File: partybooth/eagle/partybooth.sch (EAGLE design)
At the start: 21 parts, among them IC1 TINY13-20PU, IC2 78L05Z, J1 Lamp, J2 Button, J3 12V, T1 2N3904, T2 2N3904, X1 1501_06

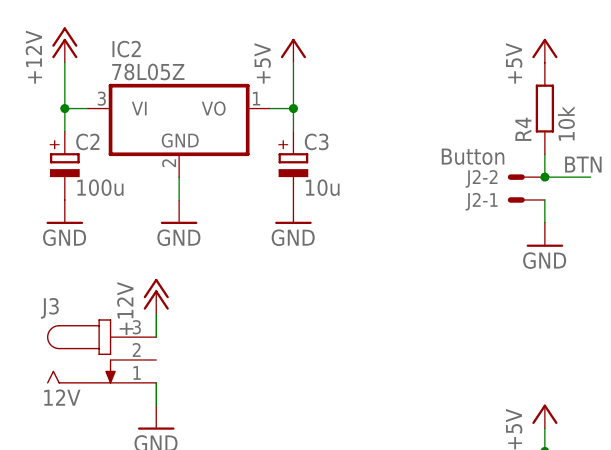
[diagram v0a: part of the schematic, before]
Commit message: 
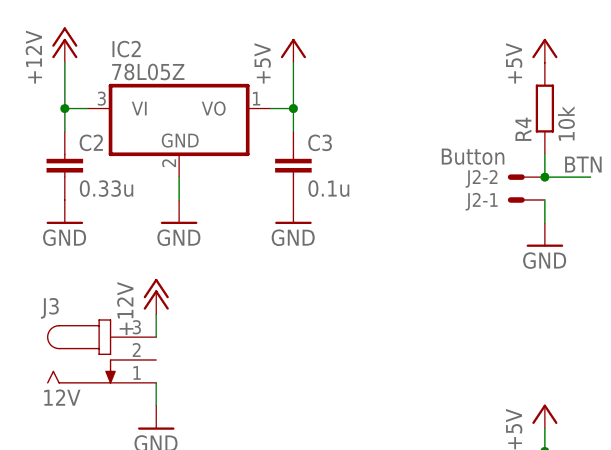
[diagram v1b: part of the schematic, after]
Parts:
- C2: value 100u -> 0.33u; device rcl:CPOL-EUB45181B -> rcl:C-EU050-025X075
- C3: value 10u -> 0.1u; device rcl:CPOL-EUB45181B -> rcl:C-EU050-025X075
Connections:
- net +12V: now also C2.1; no longer C2.+
- net +5V: now also C3.1; no longer C3.+
- net GND: now also C2.2, C3.2; no longer C2.-, C3.-
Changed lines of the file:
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@@
 <grid distance="0.1" unitdist="inch" unit="inch" style="lines" multiple="1" display="no" altdistance="0.01" altunitdist="inch" altunit="inch"/>
 <layers>
-<layer number="1" name="Top" color="4" fill="1" visible="yes" active="no"/>
-<layer number="2" name="Route2" color="1" fill="3" visible="yes" active="no"/>
-<layer number="3" name="Route3" color="4" fill="3" visible="yes" active="no"/>
-<layer number="14" name="Route14" color="1" fill="6" visible="yes" active="no"/>
-<layer number="15" name="Route15" color="4" fill="6" visible="yes" active="no"/>
-<layer number="16" name="Bottom" color="1" fill="1" visible="yes" active="no"/>
-<layer number="17" name="Pads" color="2" fill="1" visible="yes" active="no"/>
-<layer number="18" name="Vias" color="2" fill="1" visible="yes" active="no"/>
-<layer number="19" name="Unrouted" color="6" fill="1" visible="yes" active="no"/>
-<layer number="20" name="Dimension" color="15" fill="1" visible="yes" active="no"/>
-<layer number="21" name="tPlace" color="7" fill="1" visible="yes" active="no"/>
-<layer number="22" name="bPlace" color="7" fill="1" visible="yes" active="no"/>
-<layer number="23" name="tOrigins" color="15" fill="1" visible="yes" active="no"/>
-<layer number="24" name="bOrigins" color="15" fill="1" visible="yes" active="no"/>
-<layer number="25" name="tNames" color="7" fill="1" visible="yes" active="no"/>
-<layer number="26" name="bNames" color="7" fill="1" visible="yes" active="no"/>
-<layer number="27" name="tValues" color="7" fill="1" visible="yes" active="no"/>
-<layer number="28" name="bValues" color="7" fill="1" visible="yes" active="no"/>
+<layer number="1" name="Top" color="4" fill="1" visible="no" active="no"/>
+<layer number="2" name="Route2" color="1" fill="3" visible="no" active="no"/>
+<layer number="3" name="Route3" color="4" fill="3" visible="no" active="no"/>
+<layer number="14" name="Route14" color="1" fill="6" visible="no" active="no"/>
+<layer number="15" name="Route15" color="4" fill="6" visible="no" active="no"/>
+<layer number="16" name="Bottom" color="1" fill="1" visible="no" active="no"/>
+<layer number="17" name="Pads" color="2" fill="1" visible="no" active="no"/>
+<layer number="18" name="Vias" color="2" fill="1" visible="no" active="no"/>
+<layer number="19" name="Unrouted" color="6" fill="1" visible="no" active="no"/>
+<layer number="20" name="Dimension" color="15" fill="1" visible="no" active="no"/>
+<layer number="21" name="tPlace" color="7" fill="1" visible="no" active="no"/>
+<layer number="22" name="bPlace" color="7" fill="1" visible="no" active="no"/>
+<layer number="23" name="tOrigins" color="15" fill="1" visible="no" active="no"/>
+<layer number="24" name="bOrigins" color="15" fill="1" visible="no" active="no"/>
+<layer number="25" name="tNames" color="7" fill="1" visible="no" active="no"/>
+<layer number="26" name="bNames" color="7" fill="1" visible="no" active="no"/>
+<layer number="27" name="tValues" color="7" fill="1" visible="no" active="no"/>
+<layer number="28" name="bValues" color="7" fill="1" visible="no" active="no"/>
 <layer number="29" name="tStop" color="7" fill="3" visible="no" active="no"/>
 <layer number="30" name="bStop" color="7" fill="6" visible="no" active="no"/>
@@
 <layer number="35" name="tGlue" color="7" fill="4" visible="no" active="no"/>
 <layer number="36" name="bGlue" color="7" fill="5" visible="no" active="no"/>
-<layer number="37" name="tTest" color="7" fill="1" visible="yes" active="no"/>
-<layer number="38" name="bTest" color="7" fill="1" visible="yes" active="no"/>
+<layer number="37" name="tTest" color="7" fill="1" visible="no" active="no"/>
+<layer number="38" name="bTest" color="7" fill="1" visible="no" active="no"/>
 <layer number="39" name="tKeepout" color="4" fill="11" visible="no" active="no"/>
 <layer number="40" name="bKeepout" color="1" fill="11" visible="no" active="no"/>
@@
 <layer number="44" name="Drills" color="7" fill="1" visible="no" active="no"/>
 <layer number="45" name="Holes" color="7" fill="1" visible="no" active="no"/>
-<layer number="46" name="Milling" color="3" fill="1" visible="yes" active="no"/>
-<layer number="47" name="Measures" color="7" fill="1" visible="yes" active="no"/>
-<layer number="48" name="Document" color="7" fill="1" visible="yes" active="no"/>
-<layer number="49" name="Reference" color="7" fill="1" visible="yes" active="no"/>
-<layer number="51" name="tDocu" color="7" fill="1" visible="yes" active="no"/>
-<layer number="52" name="bDocu" color="7" fill="1" visible="yes" active="no"/>
+<layer number="46" name="Milling" color="3" fill="1" visible="no" active="no"/>
+<layer number="47" name="Measures" color="7" fill="1" visible="no" active="no"/>
+<layer number="48" name="Document" color="7" fill="1" visible="no" active="no"/>
+<layer number="49" name="Reference" color="7" fill="1" visible="no" active="no"/>
+<layer number="51" name="tDocu" color="7" fill="1" visible="no" active="no"/>
+<layer number="52" name="bDocu" color="7" fill="1" visible="no" active="no"/>
 <layer number="91" name="Nets" color="2" fill="1" visible="yes" active="yes"/>
 <layer number="92" name="Busses" color="1" fill="1" visible="yes" active="yes"/>
@@
 <part name="GND6" library="supply1" deviceset="GND" device=""/>
 <part name="IC2" library="linear" deviceset="78*" device="Z" technology="L05"/>
-<part name="C2" library="rcl" deviceset="CPOL-EU" device="B45181B" value="100u"/>
-<part name="C3" library="rcl" deviceset="CPOL-EU" device="B45181B" value="10u"/>
+<part name="C2" library="rcl" deviceset="C-EU" device="050-025X075" value="0.33u"/>
+<part name="C3" library="rcl" deviceset="C-EU" device="050-025X075" value="0.1u"/>
 <part name="GND7" library="supply1" deviceset="GND" device=""/>
 <part name="GND8" library="supply1" deviceset="GND" device=""/>
@@
 </segment>
 <segment>
-<pinref part="C2" gate="G$1" pin="-"/>
+<pinref part="C2" gate="G$1" pin="2"/>
 <pinref part="GND7" gate="1" pin="GND"/>
 </segment>
 <segment>
-<pinref part="C3" gate="G$1" pin="-"/>
+<pinref part="C3" gate="G$1" pin="2"/>
 <pinref part="GND9" gate="1" pin="GND"/>
 </segment>
@@
 </segment>
 <segment>
-<pinref part="C3" gate="G$1" pin="+"/>
+<pinref part="C3" gate="G$1" pin="1"/>
 <pinref part="P+6" gate="1" pin="+5V"/>
 <wire x1="-43.18" y1="101.6" x2="-43.18" y2="104.14" width="0.1524" layer="91"/>
@@
 </segment>
 <segment>
-<pinref part="C2" gate="G$1" pin="+"/>
+<pinref part="C2" gate="G$1" pin="1"/>
 <pinref part="P+7" gate="1" pin="+12V"/>
 <wire x1="-68.58" y1="101.6" x2="-68.58" y2="104.14" width="0.1524" layer="91"/>

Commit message: Check upload integrity digest, and use java.util.logging instead of System.out
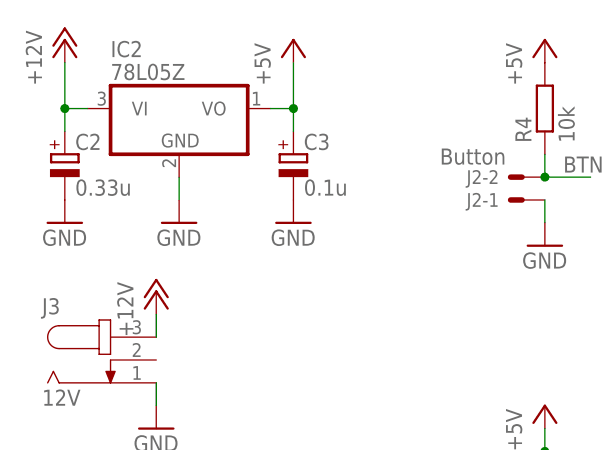
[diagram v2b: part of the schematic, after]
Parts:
- C2: device rcl:C-EU050-025X075 -> rcl:CPOL-EUE5-6
- C3: device rcl:C-EU050-025X075 -> rcl:CPOL-EUE5-5
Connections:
- net +12V: now also C2.+; no longer C2.1
- net +5V: now also C3.+; no longer C3.1
- net GND: now also C2.-, C3.-; no longer C2.2, C3.2
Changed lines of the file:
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@@
 <?xml version="1.0" encoding="utf-8"?>
 <!DOCTYPE eagle SYSTEM "eagle.dtd">
-<eagle version="6.1">
+<eagle version="6.2">
 <drawing>
 <settings>
@@
 <part name="GND6" library="supply1" deviceset="GND" device=""/>
 <part name="IC2" library="linear" deviceset="78*" device="Z" technology="L05"/>
-<part name="C2" library="rcl" deviceset="C-EU" device="050-025X075" value="0.33u"/>
-<part name="C3" library="rcl" deviceset="C-EU" device="050-025X075" value="0.1u"/>
+<part name="C2" library="rcl" deviceset="CPOL-EU" device="E5-6" value="0.33u"/>
+<part name="C3" library="rcl" deviceset="CPOL-EU" device="E5-5" value="0.1u"/>
 <part name="GND7" library="supply1" deviceset="GND" device=""/>
 <part name="GND8" library="supply1" deviceset="GND" device=""/>
@@
 </segment>
 <segment>
-<pinref part="C2" gate="G$1" pin="2"/>
+<pinref part="C2" gate="G$1" pin="-"/>
 <pinref part="GND7" gate="1" pin="GND"/>
 </segment>
 <segment>
-<pinref part="C3" gate="G$1" pin="2"/>
+<pinref part="C3" gate="G$1" pin="-"/>
 <pinref part="GND9" gate="1" pin="GND"/>
 </segment>
@@
 </segment>
 <segment>
-<pinref part="C3" gate="G$1" pin="1"/>
+<pinref part="C3" gate="G$1" pin="+"/>
 <pinref part="P+6" gate="1" pin="+5V"/>
 <wire x1="-43.18" y1="101.6" x2="-43.18" y2="104.14" width="0.1524" layer="91"/>
@@
 </segment>
 <segment>
-<pinref part="C2" gate="G$1" pin="1"/>
+<pinref part="C2" gate="G$1" pin="+"/>
 <pinref part="P+7" gate="1" pin="+12V"/>
 <wire x1="-68.58" y1="101.6" x2="-68.58" y2="104.14" width="0.1524" layer="91"/>

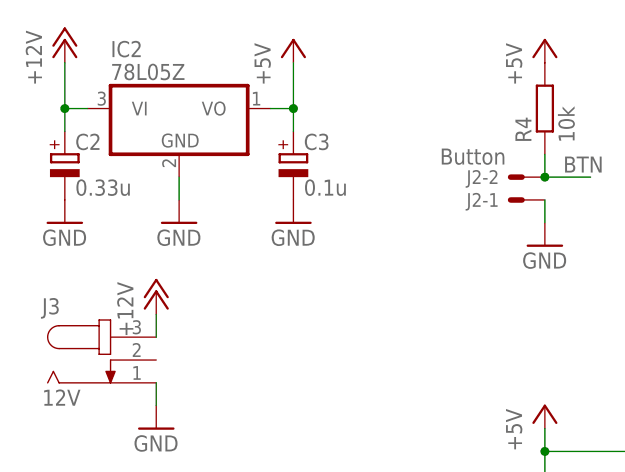
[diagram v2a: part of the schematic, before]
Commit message: 
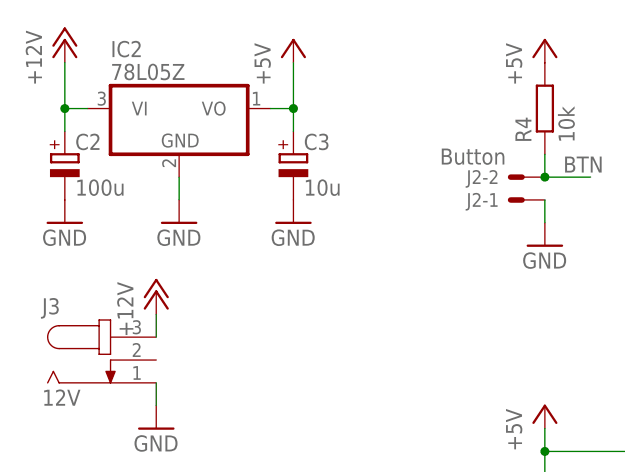
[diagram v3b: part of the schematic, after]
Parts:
- C2: value 0.33u -> 100u
- C3: value 0.1u -> 10u
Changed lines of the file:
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@@
 <part name="GND6" library="supply1" deviceset="GND" device=""/>
 <part name="IC2" library="linear" deviceset="78*" device="Z" technology="L05"/>
-<part name="C2" library="rcl" deviceset="CPOL-EU" device="E5-6" value="0.33u"/>
-<part name="C3" library="rcl" deviceset="CPOL-EU" device="E5-5" value="0.1u"/>
+<part name="C2" library="rcl" deviceset="CPOL-EU" device="E5-6" value="100u"/>
+<part name="C3" library="rcl" deviceset="CPOL-EU" device="E5-5" value="10u"/>
 <part name="GND7" library="supply1" deviceset="GND" device=""/>
 <part name="GND8" library="supply1" deviceset="GND" device=""/>
